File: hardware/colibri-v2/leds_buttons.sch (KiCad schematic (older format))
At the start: 42 parts

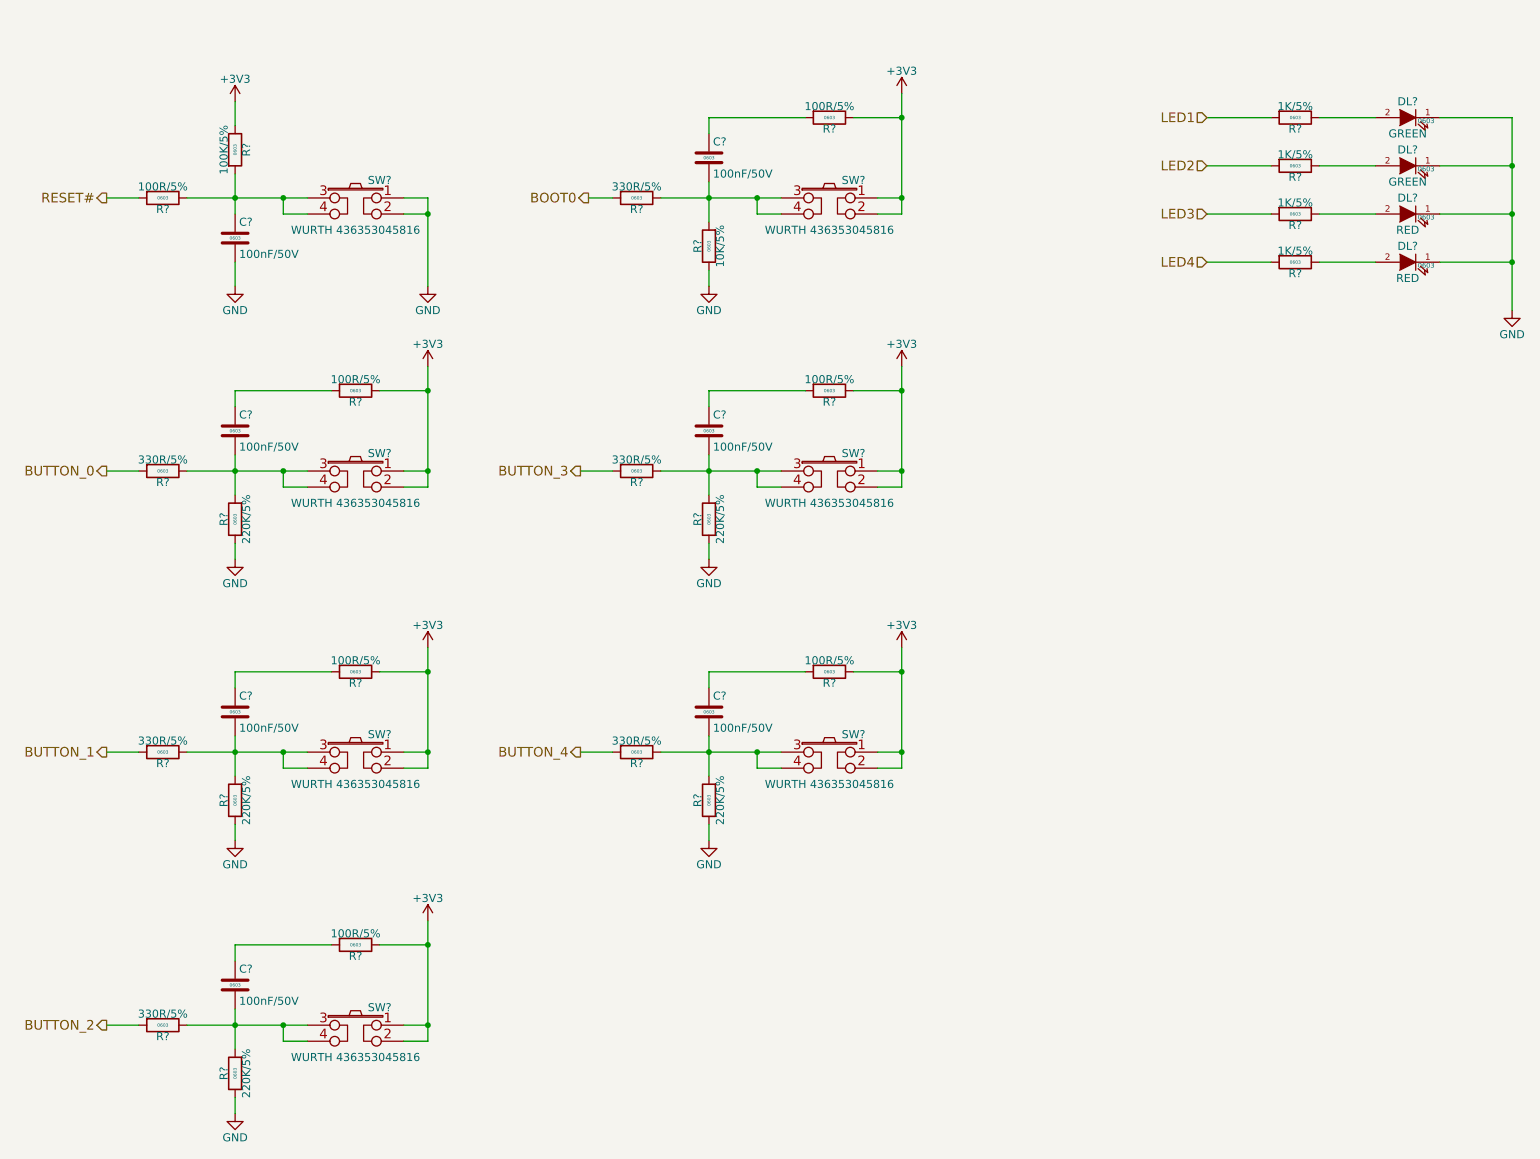
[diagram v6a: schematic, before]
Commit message: Work on power controll, buttons
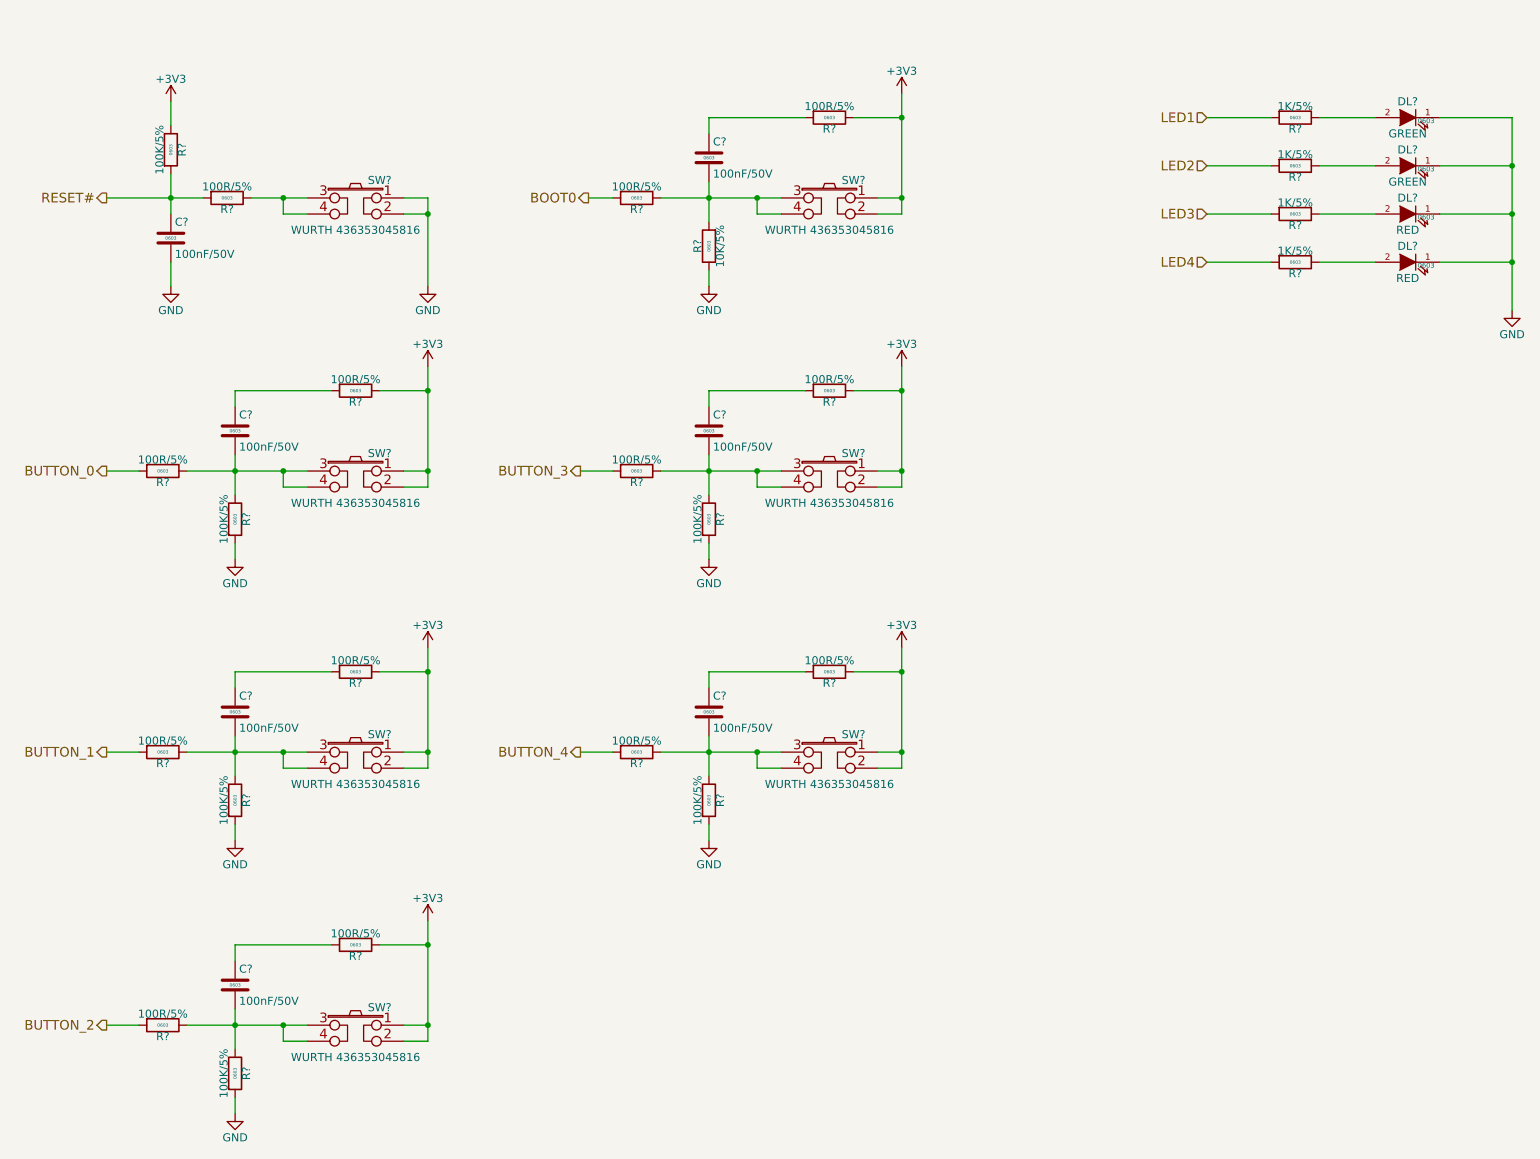
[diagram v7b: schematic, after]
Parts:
- removed R? (x6): 330R/5%, Resistors_SMD:R_0603, symbol R_SMT
- removed R? (x5): 220K/5%, Resistors_SMD:R_0603, symbol R_SMT
- added R? (x6): 100R/5%, Resistors_SMD:R_0603, symbol R_SMT
- added R? (x5): 100K/5%, Resistors_SMD:R_0603, symbol R_SMT
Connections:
- net BOOT0: now also R?.2
- net BUTTON_0: now also R?.2
- net BUTTON_1: now also R?.2
- net BUTTON_2: now also R?.2
- net BUTTON_3: now also R?.2
- net BUTTON_4: now also R?.2
- net GND: now also R?.2, R?.2, R?.2, R?.2, R?.2
- net RESET#: now also C?.1, R?.2
- net at R?.1, SW?.3, SW?.4: no longer C?.1, R?.2
- net at C?.2, SW?.3, SW?.4: now also R?.1, R?.1 (x5)
- net at C?.2, R?.2, SW?.3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: now also R?.1
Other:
- moved on the sheet: C?, R?

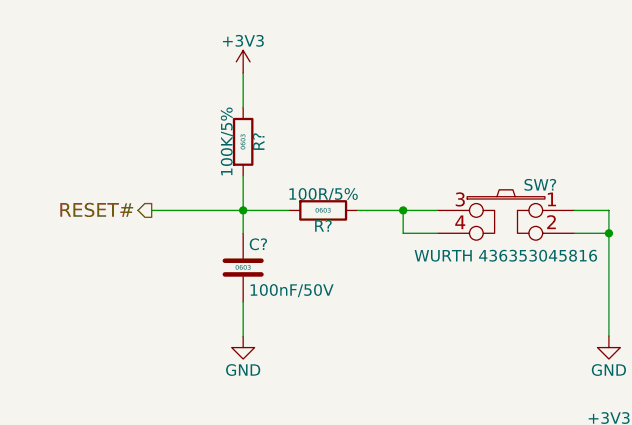
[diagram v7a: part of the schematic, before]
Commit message: Added voltage monitor TLV803SDBZT
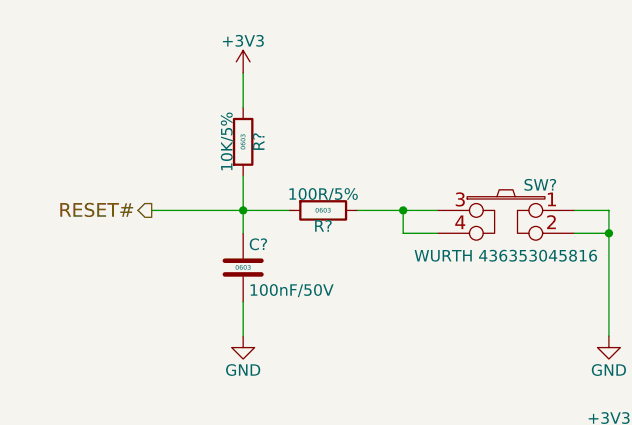
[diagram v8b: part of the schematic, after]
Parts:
- removed R?: 100K/5%, Resistors_SMD:R_0603, symbol R_SMT
- added R?: 10K/5%, Resistors_SMD:R_0603, symbol R_SMT
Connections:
- net +3V3: now also R?.1
- net RESET#: now also R?.2
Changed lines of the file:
@@
-$Comp
-L R_SMT R?
-U 1 1 56287779
-P 1750 1400
-F 0 "R?" V 1820 1400 50  0000 C CNN
-F 1 "100K/5%" V 1680 1400 50  0000 C CNN
-F 2 "Resistors_SMD:R_0603" V 1900 1400 30  0001 C CNN
-F 3 "" V 1830 1400 30  0000 C CNN
-F 4 "0603" V 1750 1400 20  0000 C CNN "SMT"
-F 5 "9233628" V 1950 1400 30  0001 C CNN "Part"
-F 6 "Farnell" V 2000 1400 30  0001 C CNN "Provider"
-	1    1750 1400
-	1    0    0    -1
-$EndComp
 $Comp
 L R_SMT R?
@@
 Wire Wire Line
 	2250 1700 2600 1700
+$Comp
+L R_SMT R?
+U 1 1 565EFB60
+P 1750 1400
+F 0 "R?" V 1820 1400 50  0000 C CNN
+F 1 "10K/5%" V 1680 1400 50  0000 C CNN
+F 2 "Resistors_SMD:R_0603" V 1900 1400 30  0001 C CNN
+F 3 "" V 1830 1400 30  0000 C CNN
+F 4 "0603" V 1750 1400 20  0000 C CNN "SMT"
+F 5 "9331700" V 1950 1400 30  0001 C CNN "Part"
+F 6 "Farnell" V 2000 1400 30  0001 C CNN "Provider"
+	1    1750 1400
+	1    0    0    -1
+$EndComp
 $EndSCHEMATC
